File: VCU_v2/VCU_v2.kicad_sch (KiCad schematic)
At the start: 0 parts

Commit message: a milli by lil wayne
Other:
- added sheet BSPD-Logic (bspd.kicad_sch)
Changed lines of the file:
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@@
+	)
+	(sheet
+		(at 191.77 73.66)
+		(size 21.59 12.7)
+		(exclude_from_sim no)
+		(in_bom yes)
+		(on_board yes)
+		(dnp no)
+		(fields_autoplaced yes)
+		(stroke
+			(width 0.1524)
+			(type solid)
+		)
+		(fill
+			(color 0 0 0 0.0000)
+		)
+		(property "Sheetname" "BSPD-Logic"
+			(at 191.77 72.9484 0)
+			(effects
+				(font
+					(size 1.27 1.27)
+				)
+				(justify left bottom)
+			)
+		)
+		(property "Sheetfile" "bspd.kicad_sch"
+			(at 191.77 86.9446 0)
+			(effects
+				(font
+					(size 1.27 1.27)
+				)
+				(justify left top)
+			)
+		)
+		(instances
+			(project "VCU_v2"
+				(path "/4ee6c2ad-9a1b-4276-b3cf-1cc8dc52967e"
+					(page "16")
+				)
+			)
+		)
 	)
 	(sheet

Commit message: bspd schematic done
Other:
- sheet BSPD-Logic ports: added BSE, BSPD-OUT, Isense-active, Isense-thresh; removed none

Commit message: vcu v2 schematics done
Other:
- sheet Connector-Root ports: added Isense-active, Isense-thresh; removed GPIO_12, GPIO_15, GPIO_16, GPIO_17, GPIO_18, GPIO_7, GPIO_8
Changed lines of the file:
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@@
 	(wire
 		(pts
-			(xy 205.74 247.65) (xy 217.17 247.65)
+			(xy 205.74 247.65) (xy 224.79 247.65)
 		)
 		(stroke
@@
 	(wire
 		(pts
+			(xy 205.74 255.27) (xy 224.79 255.27)
+		)
+		(stroke
+			(width 0)
+			(type default)
+		)
+	)
+	(wire
+		(pts
 			(xy 132.08 237.49) (xy 171.45 237.49)
 		)
@@
 	(wire
 		(pts
+			(xy 200.66 266.7) (xy 224.79 266.7)
+		)
+		(stroke
+			(width 0)
+			(type default)
+		)
+	)
+	(wire
+		(pts
 			(xy 132.08 172.72) (xy 171.45 172.72)
 		)
@@
 	(wire
 		(pts
+			(xy 200.66 262.89) (xy 224.79 262.89)
+		)
+		(stroke
+			(width 0)
+			(type default)
+		)
+	)
+	(wire
+		(pts
 			(xy 132.08 134.62) (xy 171.45 134.62)
 		)
@@
 			(width 0)
 			(type default)
+		)
+	)
+	(label "BSPD-FAULT"
+		(at 144.78 191.77 0)
+		(effects
+			(font
+				(size 1.27 1.27)
+			)
+			(justify left bottom)
+		)
+	)
+	(label "BSPD-FAULT"
+		(at 205.74 255.27 0)
+		(effects
+			(font
+				(size 1.27 1.27)
+			)
+			(justify left bottom)
+		)
+	)
+	(label "BSE-SIG"
+		(at 144.78 214.63 0)
+		(effects
+			(font
+				(size 1.27 1.27)
+			)
+			(justify left bottom)
 		)
 	)
@@
 		(dnp no)
 		(fields_autoplaced yes)
-		(property "Reference" "#PWR02"
+		(property "Reference" "#PWR03"
 			(at 207.01 232.41 0)
 			(effects
@@
 			(project ""
 				(path "/4ee6c2ad-9a1b-4276-b3cf-1cc8dc52967e"
-					(reference "#PWR02")
+					(reference "#PWR03")
 					(unit 1)
 				)
@@
 		(on_board yes)
 		(dnp no)
-		(property "Reference" "#PWR025"
+		(property "Reference" "#PWR01"
 			(at 205.74 67.31 0)
 			(effects
@@
 			(project ""
 				(path "/4ee6c2ad-9a1b-4276-b3cf-1cc8dc52967e"
-					(reference "#PWR025")
+					(reference "#PWR01")
 					(unit 1)
 				)
@@
 		(dnp no)
 		(fields_autoplaced yes)
-		(property "Reference" "#PWR01"
+		(property "Reference" "#PWR02"
 			(at 207.01 198.12 0)
 			(effects
@@
 			(project ""
 				(path "/4ee6c2ad-9a1b-4276-b3cf-1cc8dc52967e"
-					(reference "#PWR01")
+					(reference "#PWR02")
 					(unit 1)
 				)
@@
 			)
 		)
-		(pin "GPIO_8" input
-			(at 171.45 60.96 180)
-			(effects
-				(font
-					(size 1.27 1.27)
-				)
-				(justify left)
-			)
-		)
 		(pin "GPIO_9" input
 			(at 171.45 64.77 180)
@@
 			)
 		)
-		(pin "GPIO_7" input
-			(at 171.45 57.15 180)
-			(effects
-				(font
-					(size 1.27 1.27)
-				)
-				(justify left)
-			)
-		)
 		(pin "GPIO_20" input
 			(at 171.45 106.68 180)
@@
 			)
 		)
-		(pin "GPIO_16" input
-			(at 171.45 91.44 180)
-			(effects
-				(font
-					(size 1.27 1.27)
-				)
-				(justify left)
-			)
-		)
 		(pin "GPIO_19" input
 			(at 171.45 102.87 180)
@@
 			)
 		)
-		(pin "GPIO_12" input
-			(at 171.45 76.2 180)
-			(effects
-				(font
-					(size 1.27 1.27)
-				)
-				(justify left)
-			)
-		)
-		(pin "GPIO_17" input
-			(at 171.45 95.25 180)
-			(effects
-				(font
-					(size 1.27 1.27)
-				)
-				(justify left)
-			)
-		)
-		(pin "GPIO_18" input
-			(at 171.45 99.06 180)
-			(effects
-				(font
-					(size 1.27 1.27)
-				)
-				(justify left)
-			)
-		)
-		(pin "GPIO_15" input
-			(at 171.45 87.63 180)
-			(effects
-				(font
-					(size 1.27 1.27)
-				)
-				(justify left)
-			)
-		)
 		(pin "GPIO_PWM_4" input
 			(at 171.45 45.72 180)
@@
 		(pin "Vin+" input
 			(at 200.66 53.34 0)
+			(effects
+				(font
+					(size 1.27 1.27)
+				)
+				(justify right)
+			)
+		)
+		(pin "Isense-active" input
+			(at 200.66 266.7 0)
+			(effects
+				(font
+					(size 1.27 1.27)
+				)
+				(justify right)
+			)
+		)
+		(pin "Isense-thresh" input
+			(at 200.66 262.89 0)
 			(effects
 				(font
@@
 	)
 	(sheet
-		(at 217.17 244.1762)
+		(at 224.79 244.1762)
 		(size 22.86 26.3338)
 		(exclude_from_sim no)
@@
 		)
 		(property "Sheetname" "BSPD-Logic"
-			(at 217.17 243.4646 0)
+			(at 224.79 243.4646 0)
 			(effects
 				(font
@@
 		)
 		(property "Sheetfile" "bspd.kicad_sch"
-			(at 217.17 271.0946 0)
+			(at 224.79 271.0946 0)
 			(effects
 				(font
@@
 		)
 		(pin "Isense-thresh" input
-			(at 217.17 262.89 180)
+			(at 224.79 262.89 180)
 			(effects
 				(font
@@
 		)
 		(pin "Isense-active" input
-			(at 217.17 266.7 180)
+			(at 224.79 266.7 180)
 			(effects
 				(font
@@
 		)
 		(pin "BSPD-OUT" input
-			(at 217.17 255.27 180)
+			(at 224.79 255.27 180)
 			(effects
 				(font
@@
 		)
 		(pin "BSE" input
-			(at 217.17 247.65 180)
-			(effects
-				(font
+			(at 224.79 247.65 180)
+			(effects
+				(font

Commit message: placements friggin 80% friggin done shoutout epstein
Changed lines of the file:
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@@
-	(wire
-		(pts
-			(xy 200.66 266.7) (xy 224.79 266.7)
-		)
-		(stroke
-			(width 0)
-			(type default)
-		)
-	)
 	(wire
 		(pts
@@
 		(dnp no)
 		(fields_autoplaced yes)
-		(property "Reference" "#PWR03"
+		(property "Reference" "#PWR02"
 			(at 207.01 232.41 0)
 			(effects
@@
 			(project ""
 				(path "/4ee6c2ad-9a1b-4276-b3cf-1cc8dc52967e"
-					(reference "#PWR03")
+					(reference "#PWR02")
 					(unit 1)
 				)
@@
 		(on_board yes)
 		(dnp no)
-		(property "Reference" "#PWR01"
+		(property "Reference" "#PWR025"
 			(at 205.74 67.31 0)
 			(effects
@@
 			(project ""
 				(path "/4ee6c2ad-9a1b-4276-b3cf-1cc8dc52967e"
-					(reference "#PWR01")
+					(reference "#PWR025")
 					(unit 1)
 				)
@@
 		(dnp no)
 		(fields_autoplaced yes)
-		(property "Reference" "#PWR02"
+		(property "Reference" "#PWR01"
 			(at 207.01 198.12 0)
 			(effects
@@
 			(project ""
 				(path "/4ee6c2ad-9a1b-4276-b3cf-1cc8dc52967e"
-					(reference "#PWR02")
+					(reference "#PWR01")
 					(unit 1)
 				)

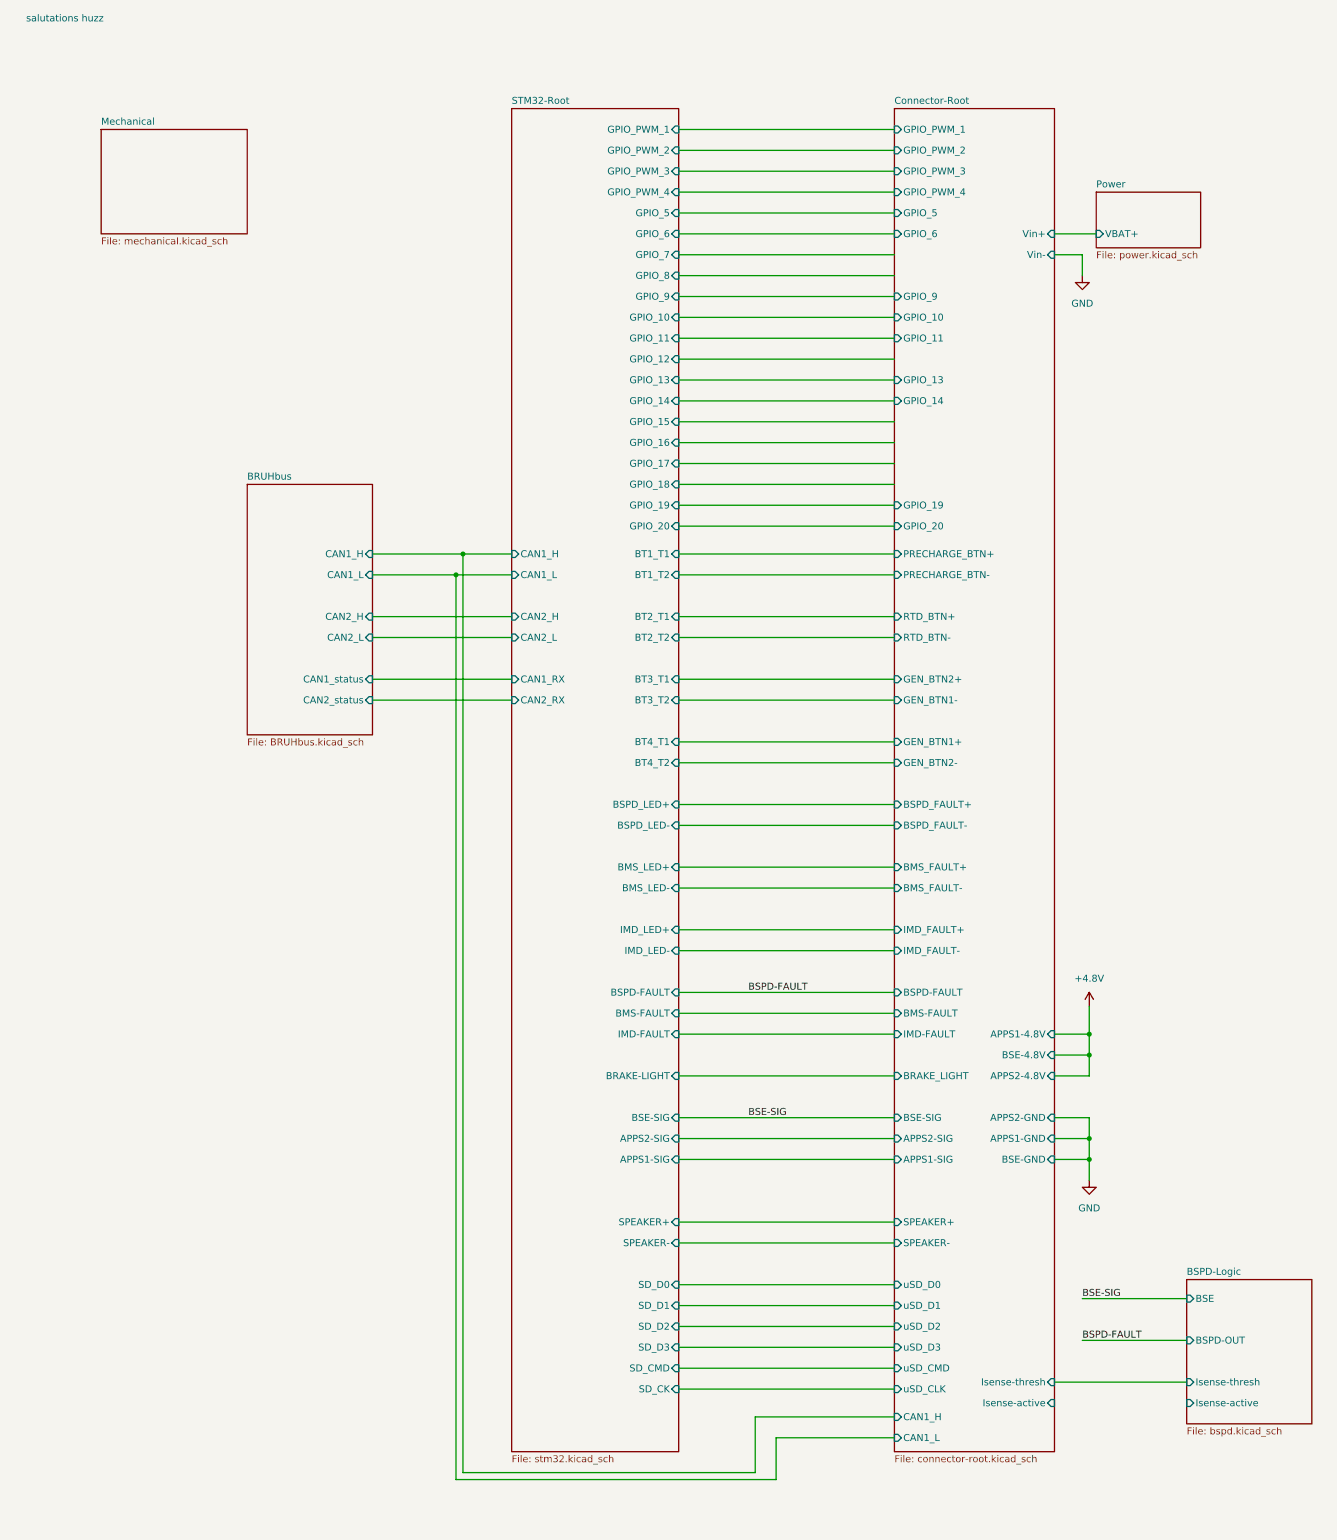
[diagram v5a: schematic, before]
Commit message: slimed ethernet
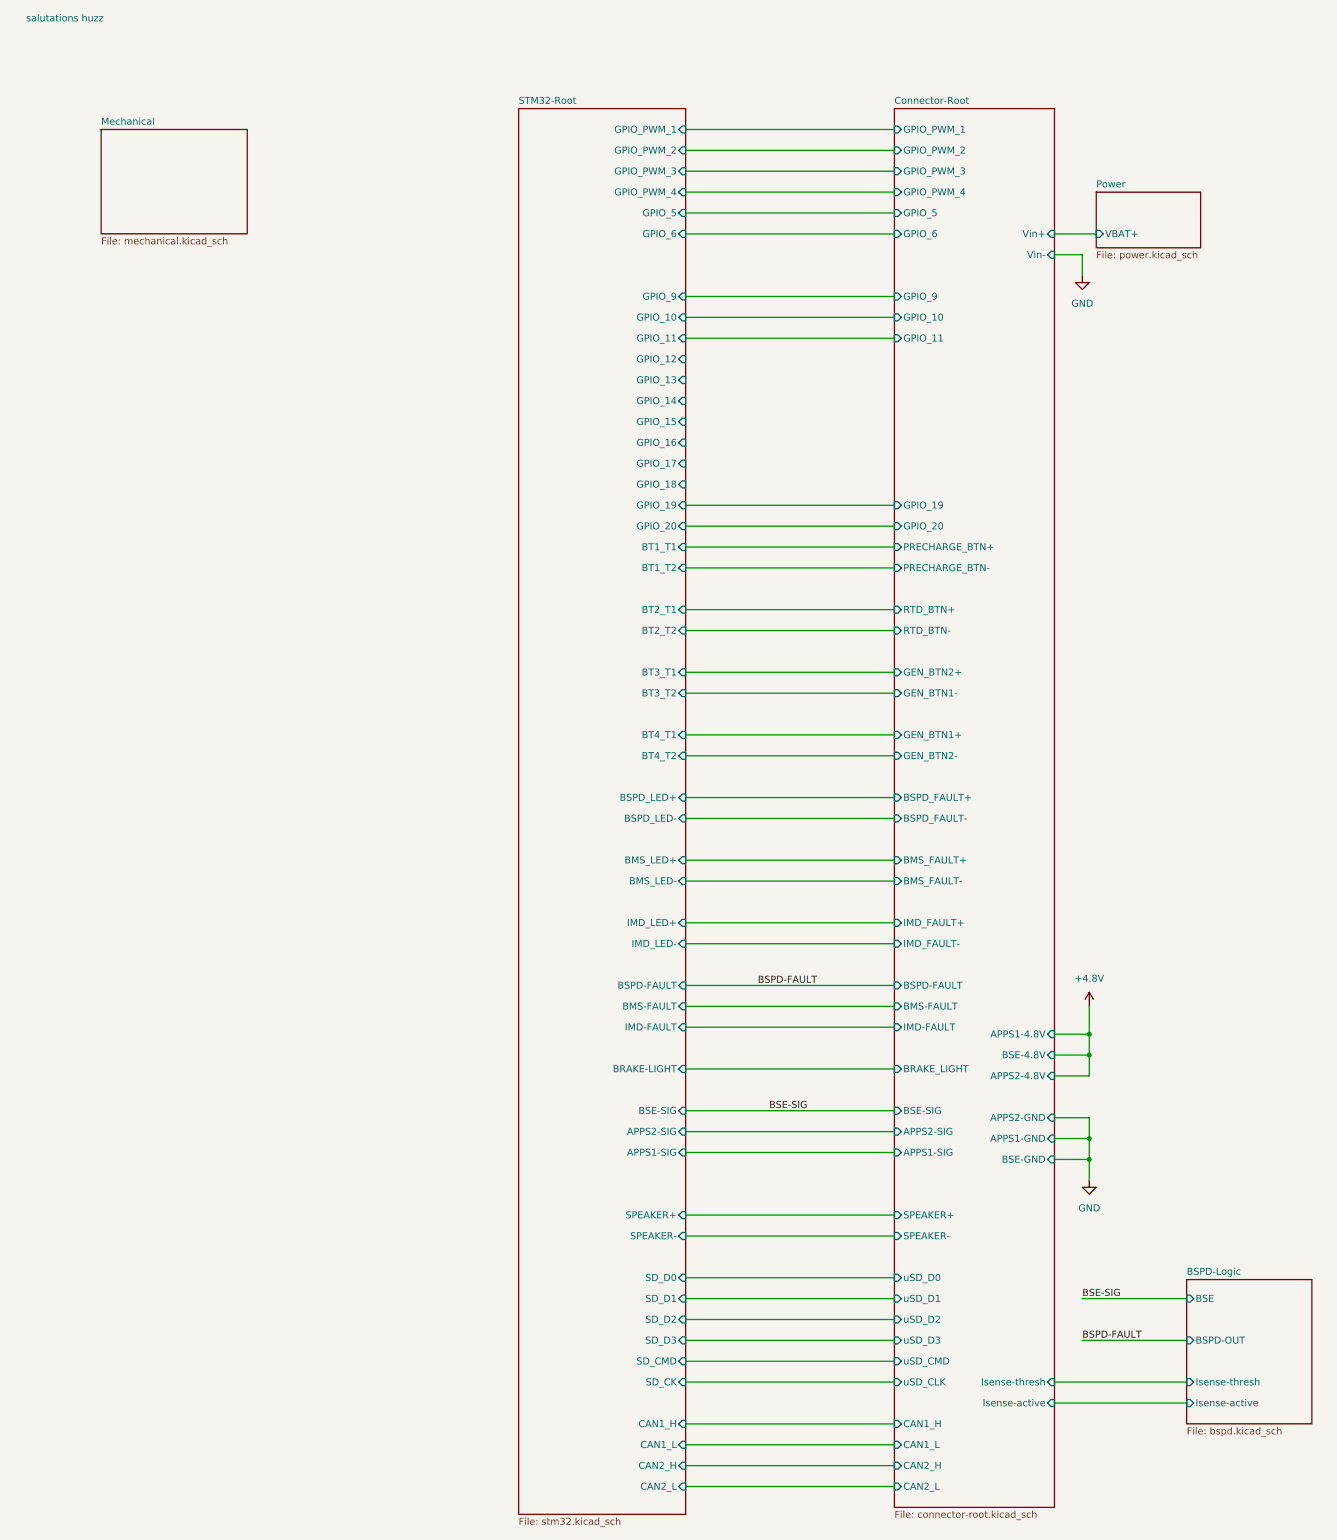
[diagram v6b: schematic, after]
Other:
- removed sheet BRUHbus
- sheet Connector-Root ports: added CAN2_H, CAN2_L; removed GPIO_13, GPIO_14
- sheet STM32-Root ports: added none; removed CAN1_RX, CAN2_RX, GPIO_7, GPIO_8

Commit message: Added connector for daq vcu
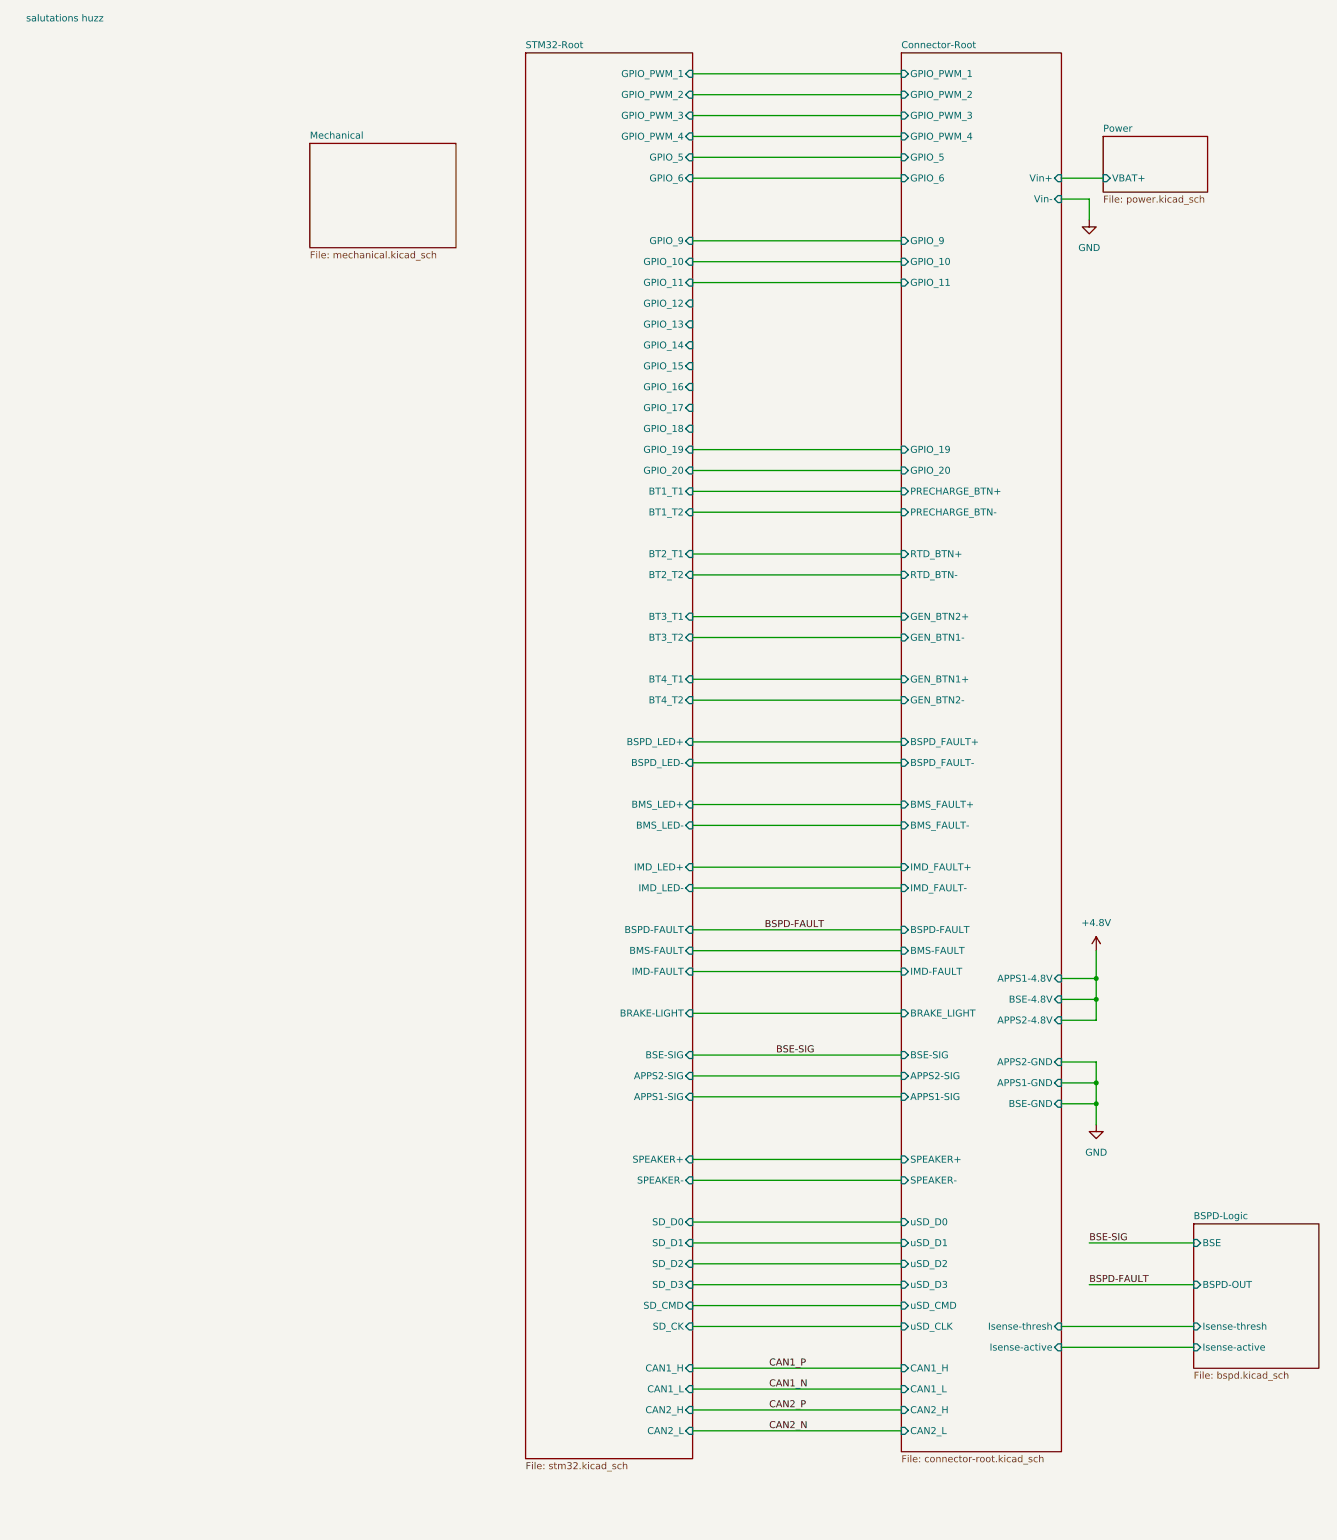
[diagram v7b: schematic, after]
